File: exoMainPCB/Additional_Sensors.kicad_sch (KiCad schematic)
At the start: 0 parts

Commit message: added power and started imu
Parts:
- added C7, C8: 22 pF, symbol Device:C
- added R10, R9: R, symbol Device:R
- added U4: BNO085, BNO085:IC_BNO085, symbol BNO085:BNO085
- added Y3: 32.768 kHz, symbol Device:Crystal
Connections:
- new net: C8.1, U4.26 (XOUT32/CLKSEL1), Y3.1
- new net: U4.1 (RESV_NC), U4.12 (RESV_NC), U4.13 (RESV_NC), U4.21 (RESV_NC), U4.22 (RESV_NC), U4.23 (RESV_NC), U4.24 (RESV_NC), U4.7 (RESV_NC), U4.8 (RESV_NC)
- new net: C7.1, U4.27 (XIN32), Y3.2
- new net +3V3: R10.1, R9.1
- new net GND: C7.2, C8.2
- new net SCL: R10.2
- new net SDA: R9.2

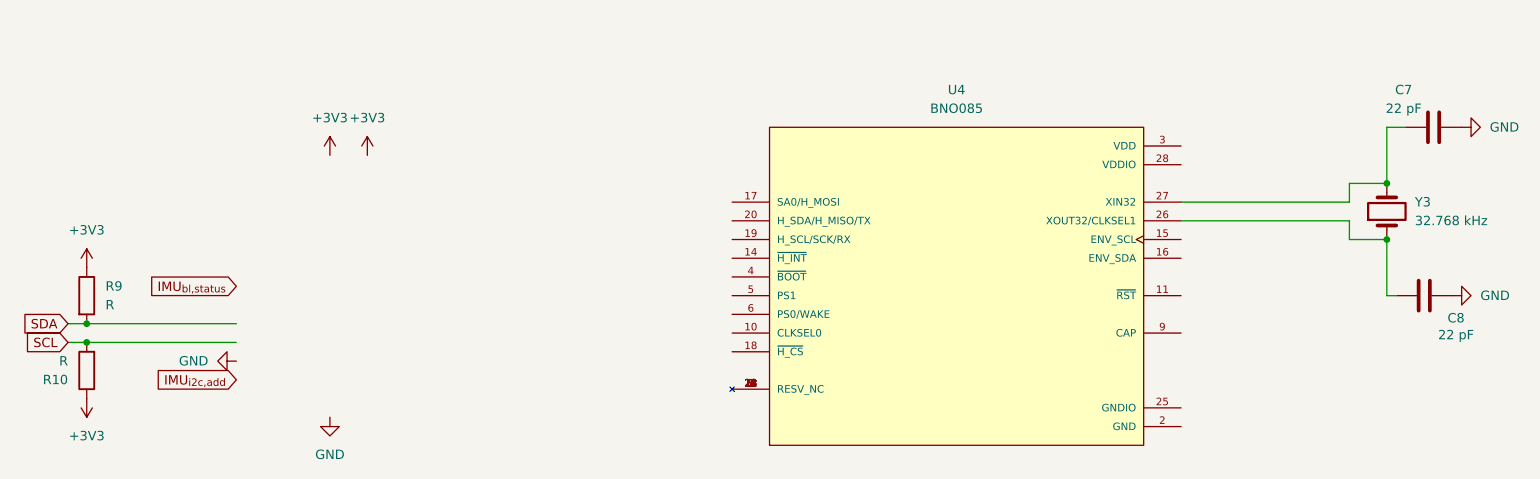
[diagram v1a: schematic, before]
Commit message: finished IMU and added component values
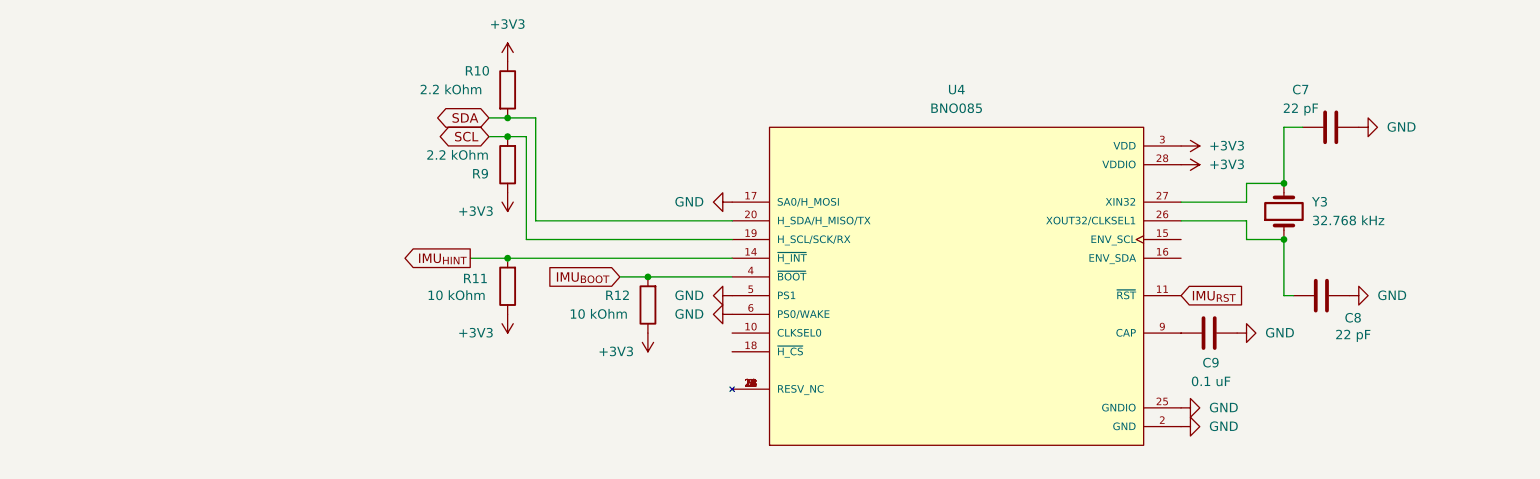
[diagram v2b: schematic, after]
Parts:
- added C9: 0.1 uF, symbol Device:C
- added R11, R12: 10 kOhm, symbol Device:R
- R10, R9: value R -> 2.2 kOhm
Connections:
- net +3V3: now also U4.28 (VDDIO), U4.3 (VDD), R11.1, R12.1
- net GND: now also U4.17 (SA0/H_MOSI), U4.2 (GND), U4.25 (GNDIO), U4.5 (PS1), U4.6 (PS0/WAKE), C9.2
- net SCL: now also R9.2, U4.19 (H_SCL/SCK/RX); no longer R10.2
- net SDA: now also R10.2, U4.20 (H_SDA/H_MISO/TX); no longer R9.2
- net IMU_{RST}: now reaches U4.11 (~{RST})
- net IMU_{HINT}: now reaches U4.14 (~{H_INT})
- net IMU_{HINT}: now also R11.2
- net IMU_{BOOT}: now reaches U4.4 (~{BOOT})
- net IMU_{BOOT}: now also R12.2
- net at U4.9 (CAP): now also C9.1
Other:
- moved on the sheet: C7, C8, Y3

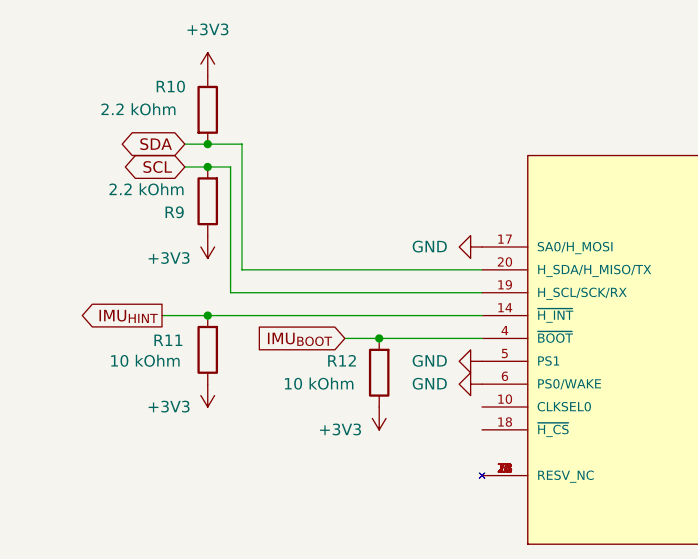
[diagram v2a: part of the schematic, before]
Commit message: changed all resistors to US, updated IO, finished Handheld
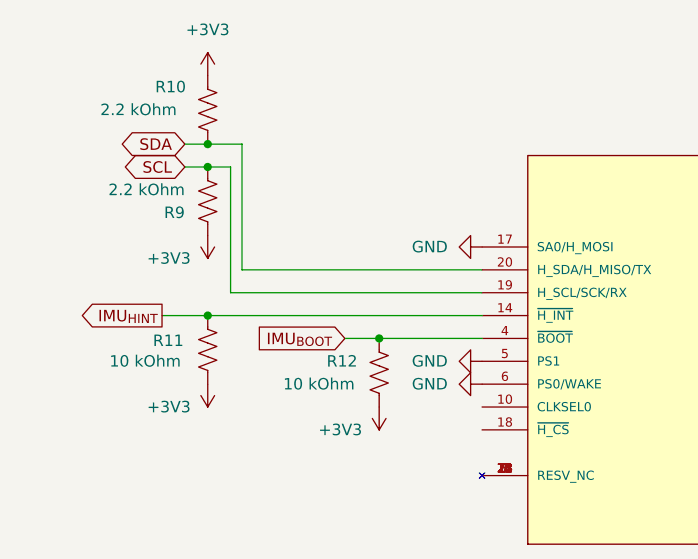
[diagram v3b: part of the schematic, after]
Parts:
- R10, R11, R12, R9: symbol Device:R -> Device:R_US
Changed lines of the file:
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@@
 	)
 	(symbol
-		(lib_id "Device:R")
+		(lib_id "Device:R_US")
 		(at 104.14 46.99 0)
 		(unit 1)
@@
 	)
 	(symbol
-		(lib_id "Device:R")
+		(lib_id "Device:R_US")
 		(at 123.19 76.2 180)
 		(unit 1)
@@
 	)
 	(symbol
-		(lib_id "Device:R")
+		(lib_id "Device:R_US")
 		(at 104.14 57.15 180)
 		(unit 1)
@@
 	)
 	(symbol
-		(lib_id "Device:R")
+		(lib_id "Device:R_US")
 		(at 104.14 73.66 180)
 		(unit 1)
